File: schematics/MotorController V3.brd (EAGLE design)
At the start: 120.6 x 100 mm, 53 parts, among them IC1 7805, Q1 BC307

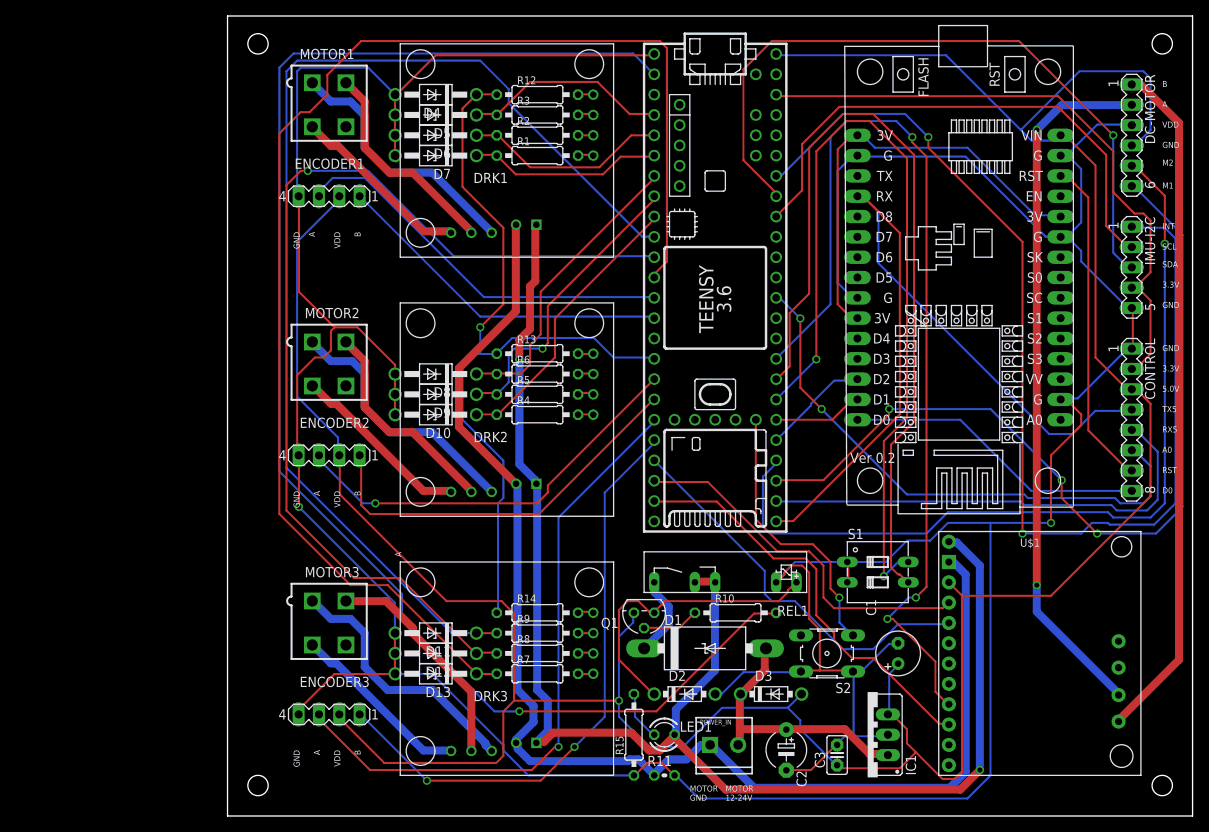
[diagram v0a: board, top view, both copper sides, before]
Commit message: ESP8266 NodeMCU V2 foot print corrected
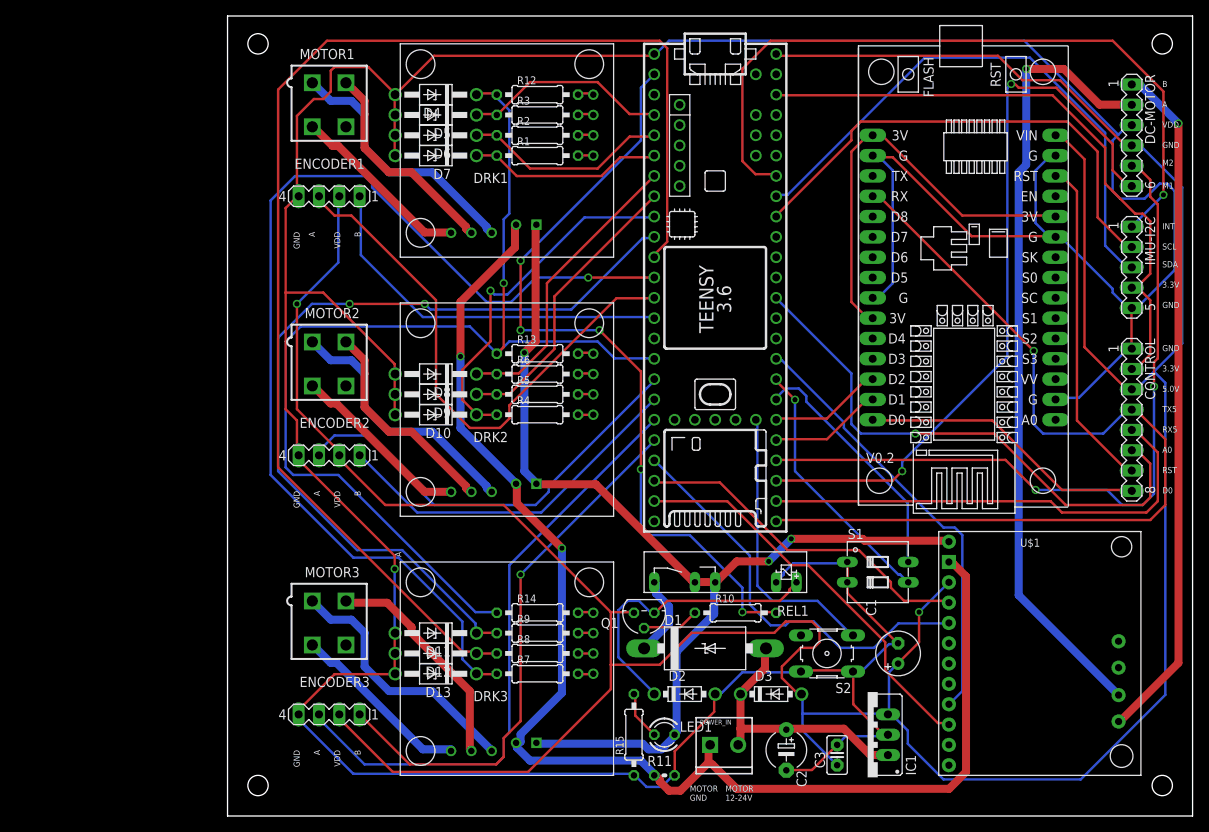
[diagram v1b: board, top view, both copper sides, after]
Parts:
- moved U$3 0.63 mm to (14.6, 53.3)
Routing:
- net N$42: track 180.6 -> 98.5 mm, vias 1 -> 5
- net N$40: track 105.1 -> 30.9 mm, vias 2 -> 0
- net N$12: track 103.3 -> 32.4 mm, vias 0 -> 1
- net N$60: track 120.2 -> 54.8 mm, vias 3 -> 0
- net LIPO-VDD: track 184.1 -> 132.3 mm, vias 2 -> 3
- net IMU-INT: track 137.9 -> 91.8 mm, vias 2 -> 1
- net +5V: track 380.7 -> 422.6 mm, vias 1 -> 2
- net N$46: track 98.7 -> 135.9 mm
- net N$28: track 125.6 -> 162.7 mm, vias 1 -> 0
- net N$27: track 141.1 -> 106.0 mm, vias 0 -> 2
- net N$29: track 167.4 -> 133.0 mm, vias 0 -> 1
- net ENC1_A: track 49.4 -> 68.8 mm
- net IMU-SDA: track 87.9 -> 70.9 mm, vias 1 -> 0
- net WH_ENC_B: track 107.0 -> 92.6 mm, vias 3 -> 2
- net GND: track 516.2 -> 503.0 mm, vias 2 -> 1
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
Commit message: calibrated PID of lifter motor
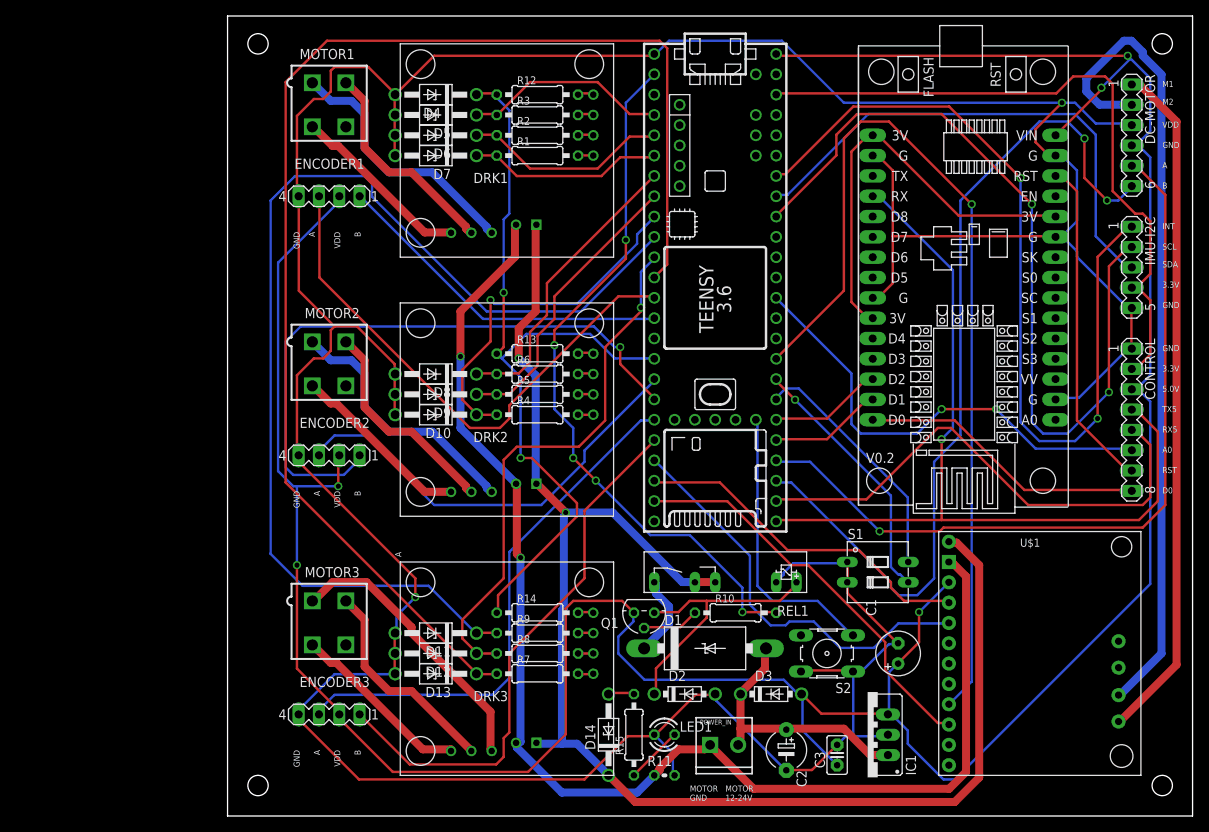
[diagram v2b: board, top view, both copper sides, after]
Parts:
- added D14: 5.6V, diode:DO41Z10
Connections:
- removed net N$41: LED1.A, R15.2
- new net N$33: D14.A, R15.2
- new net N$34: LED1.K, R15.1
- net GND: now also LED1.A; no longer R15.1
- net LIPO-VDD: now also D14.C; no longer LED1.K
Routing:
- net N$28: track 162.7 -> 67.3 mm, vias 0 -> 1
- net N$60: track 54.8 -> 115.9 mm, vias 0 -> 1
- net LIPO-VDD: track 132.3 -> 182.0 mm, vias 3 -> 2
- net IMU-SCL: track 61.5 -> 102.7 mm, vias 0 -> 2
- net N$46: track 135.9 -> 99.6 mm, vias 1 -> 2
- net ENC2_B: track 45.6 -> 78.6 mm, vias 0 -> 1
- net N$29: track 133.0 -> 165.9 mm, vias 1 -> 0
- net GND: track 503.0 -> 470.7 mm, vias 1 -> 2
- net +5V: track 422.6 -> 390.5 mm, vias 2 -> 5
- net N$27: track 106.0 -> 137.7 mm, vias 2 -> 0
- net WH_ENC_B: track 92.6 -> 109.0 mm
- net IMU-INT: track 91.8 -> 106.3 mm, vias 1 -> 2
- net A0: track 68.8 -> 58.7 mm, vias 1 -> 2
- net ENC3_A: track 76.3 -> 66.7 mm
- net N$42: track 98.5 -> 89.3 mm
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
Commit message: no message
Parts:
- removed U$3: NODEMCUNODEMCUV2, nodemcu:NODEMCUV2
- added U$2: NODEMCUNODEMCUV2, nodemcu:NODEMCUV2
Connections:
- net +5V: now also IMU-I2C.4, U$2.30; no longer U$3.15
- net 3.3V: now also IMU-I2C.5; no longer IMU-I2C.4
- net 3V: now also U$2.11, U$2.16; no longer U$3.11, U$3.16, U$3.25
- net D0: now also U$2.15; no longer U$3.30
- net GND: now also U$2.10, U$2.17, U$2.2, U$2.24, U$2.25, U$2.29, U$2.9; no longer IMU-I2C.5, U$3.10, U$3.14, U$3.17, U$3.2, U$3.24
- net RST: now also U$2.28; no longer U$3.13
- net SCL1: now also U$2.13; no longer U$3.28
- net SDA1: now also U$2.14; no longer U$3.29
- net TX5: now also U$2.4; no longer U$3.19
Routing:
- net N$29: track 165.9 -> 65.9 mm, vias 0 -> 2
- net N$12: track 32.4 -> 112.0 mm, vias 1 -> 0
- net GND: track 470.7 -> 414.8 mm, vias 2 -> 0
- net N$42: track 89.3 -> 137.7 mm, vias 5 -> 3
- net IMU-SCL: track 102.7 -> 64.1 mm, vias 2 -> 0
- net N$28: track 67.3 -> 103.9 mm, vias 1 -> 2
- net ENC2_B: track 78.6 -> 45.6 mm, vias 1 -> 0
- net N$27: track 137.7 -> 105.1 mm, vias 0 -> 2
- net +5V: track 390.5 -> 412.4 mm, vias 5 -> 2
- net IMU-INT: track 106.3 -> 92.2 mm, vias 2 -> 3
- net N$60: track 115.9 -> 128.5 mm, vias 1 -> 0
- net WH_ENC_B: track 109.0 -> 97.8 mm, vias 2 -> 1
- net BLCK-M2: track 101.3 -> 111.7 mm
- net RST: track 41.6 -> 49.8 mm, vias 0 -> 1
- net RX5: track 64.7 -> 57.0 mm
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
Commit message: no message
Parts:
- moved U$2 112.1 mm to (21.6, 50.2), turned to 180 degrees
- moved MOTOR1 90.7 mm to (-17.1, -3.81), turned to 0 degrees
- moved POWER_IN 83.2 mm to (0.00, 76.8)
- moved MOTOR2 77.1 mm to (-0.64, -3.81), turned to 0 degrees
- moved ENCODER1 72.7 mm to (-16.5, 6.99), turned to 0 degrees
- moved R15 71.3 mm to (5.71, 61.0), turned to 270 degrees
- moved D3 68.5 mm to (1.91, 69.2), turned to 180 degrees
- moved ENCODER2 66.7 mm to (0.00, 6.99), turned to 0 degrees
- moved IC1 64.7 mm to (-14.6, 57.8), turned to 0 degrees
- moved LED1 63.9 mm to (-3.17, 57.8)
- moved D14 61.3 mm to (0.64, 50.8), turned to 0 degrees
- moved R11 57.8 mm to (-8.26, 47.6), turned to 180 degrees
- moved CONTROL 55.1 mm to (-10.2, 62.2), turned to 0 degrees
- moved IMU-I2C 54.4 mm to (-14.0, 70.5), turned to 0 degrees
- moved C2 53.9 mm to (-16.5, 47.0), turned to 0 degrees
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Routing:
- net GND: track 414.8 -> 0.00 mm
- net +5V: track 412.4 -> 0.00 mm, vias 2 -> 0
- net LIPO-VDD: track 182.0 -> 0.00 mm, vias 2 -> 0
- net LIPO-GND: track 163.5 -> 0.00 mm, vias 2 -> 0
- net N$42: track 137.7 -> 0.00 mm, vias 3 -> 0
- net N$60: track 128.5 -> 0.00 mm
- net TX5: track 114.4 -> 0.00 mm
- net N$12: track 112.0 -> 0.00 mm
- net BLCK-M2: track 111.7 -> 0.00 mm
- net N$27: track 105.1 -> 0.00 mm, vias 2 -> 0
- net N$28: track 103.9 -> 0.00 mm, vias 2 -> 0
- net Y_ENC_A: track 100.2 -> 0.00 mm, vias 3 -> 0
- net WH_ENC_B: track 97.8 -> 0.00 mm, vias 1 -> 0
- net N$46: track 97.6 -> 0.00 mm, vias 1 -> 0
- net IMU-INT: track 92.2 -> 0.00 mm, vias 3 -> 0
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
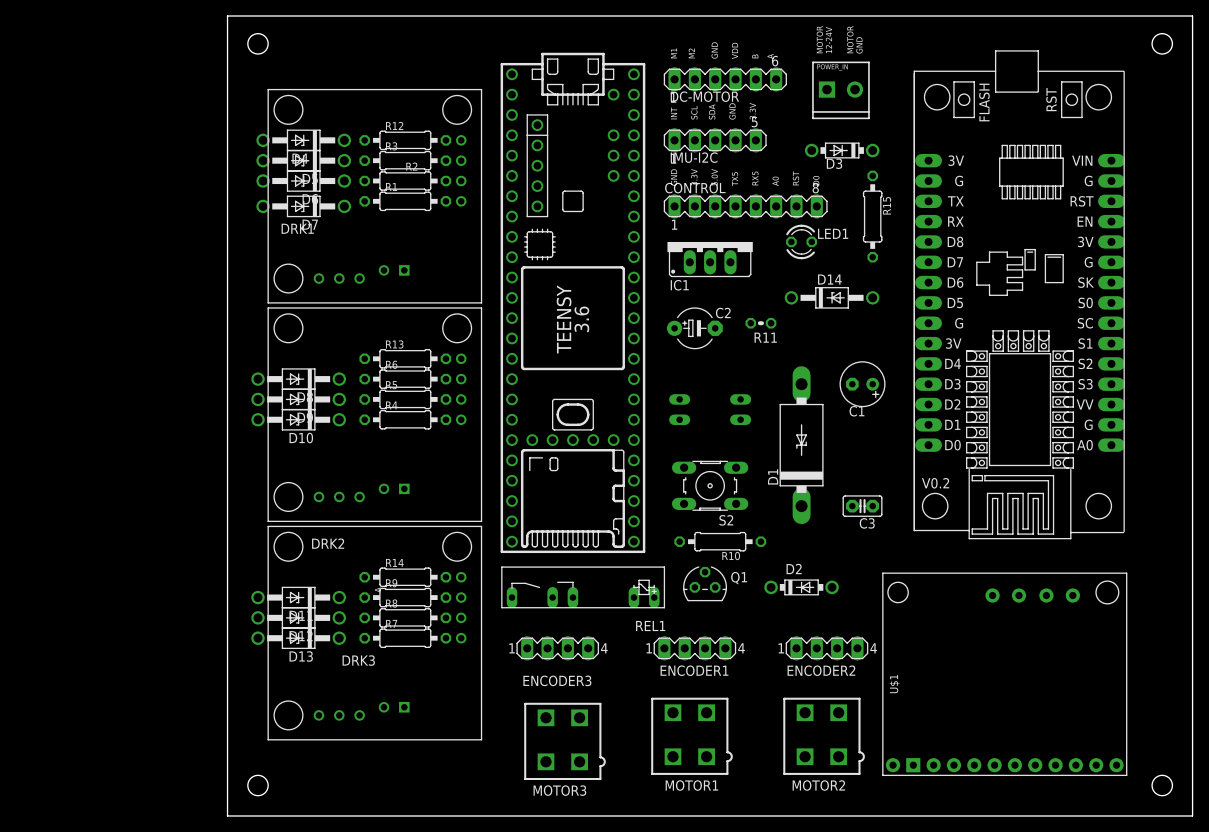
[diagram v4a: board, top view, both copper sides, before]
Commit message: more aggressive Motor PID
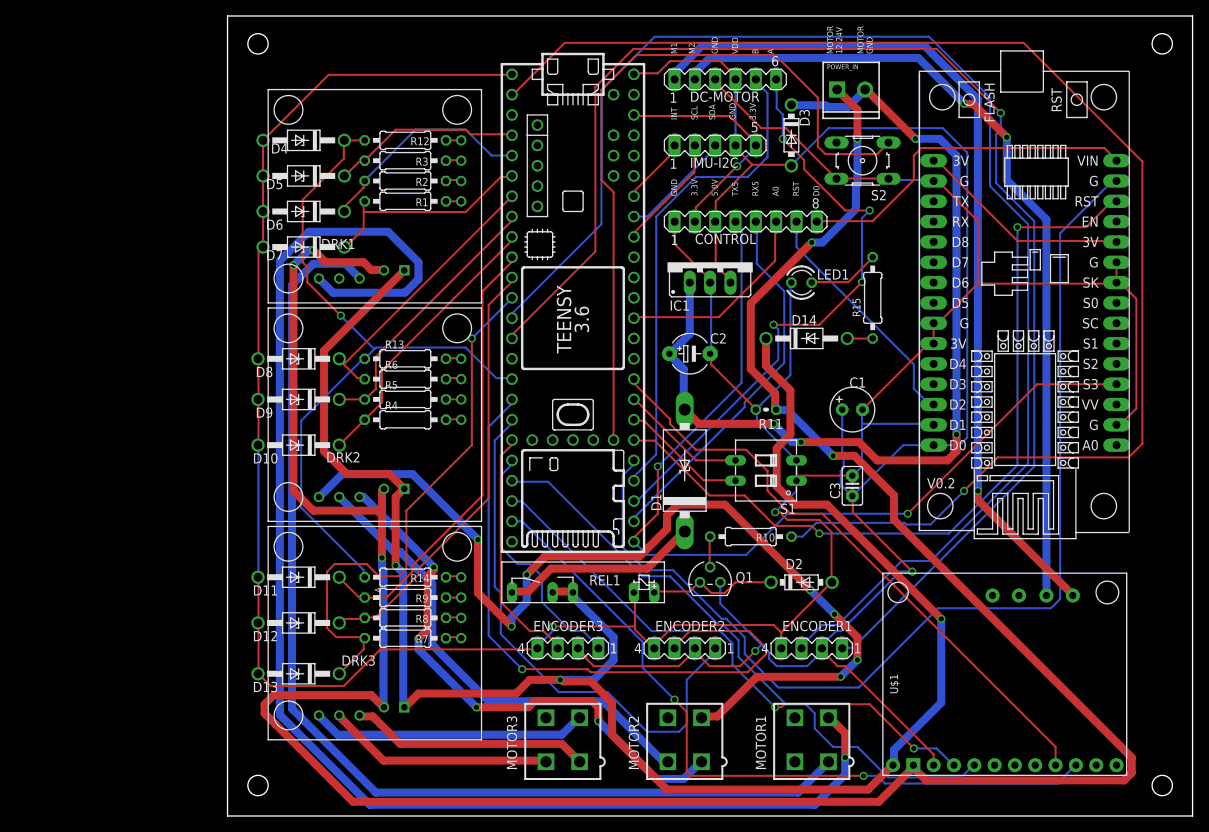
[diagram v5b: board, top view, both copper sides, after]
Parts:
- R4, R5, R6, R7, R8, R9: value 330 -> 1K
- moved S2 44.9 mm to (4.45, 67.9)
- moved ENCODER2 17.8 mm to (-17.8, 6.99), turned to 180 degrees
- moved MOTOR2 17.2 mm to (-17.8, -4.45)
- moved MOTOR1 15.3 mm to (-1.91, -4.45)
- moved D1 14.9 mm to (-17.8, 29.2)
- moved ENCODER1 14.6 mm to (-1.91, 6.99), turned to 180 degrees
- moved R11 10.8 mm to (-7.62, 36.8)
- moved S1 10.3 mm to (-7.62, 29.2), flipped to the top
- moved R15 10.2 mm to (5.71, 50.8)
- moved D3 6.63 mm to (-4.45, 71.1), turned to 270 degrees
- moved D14 5.99 mm to (-2.54, 45.7)
- moved D7 5.08 mm to (-65.4, 57.1)
- moved LED1 5.08 mm to (-3.17, 52.7)
- moved D13 4.45 mm to (-66.0, 3.81)
- moved R10 3.86 mm to (-9.53, 21.0), turned to 0 degrees
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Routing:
- net GND: track 0.00 -> 402.1 mm, vias 0 -> 2
- net LIPO-GND: track 0.00 -> 329.4 mm, vias 0 -> 6
- net +5V: track 0.00 -> 235.1 mm, vias 0 -> 2
- net LIPO-VDD: track 0.00 -> 228.6 mm, vias 0 -> 3
- net N$1: track 0.00 -> 178.1 mm, vias 0 -> 1
- net ENC1_A: track 0.00 -> 173.4 mm
- net N$42: track 0.00 -> 171.7 mm, vias 0 -> 1
- net ENC1_B: track 0.00 -> 171.6 mm, vias 0 -> 1
- net N$3: track 0.00 -> 136.3 mm
- net SDA1: track 0.00 -> 134.7 mm
- net N$13: track 0.00 -> 122.5 mm, vias 0 -> 7
- net N$32: track 0.00 -> 116.8 mm, vias 0 -> 4
- net TX5: track 0.00 -> 115.8 mm, vias 0 -> 2
- net RED-M1: track 0.00 -> 109.8 mm, vias 0 -> 1
- net BLCK-M2: track 0.00 -> 104.1 mm, vias 0 -> 2
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
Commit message: aligned coord systems of IMU and kinematics
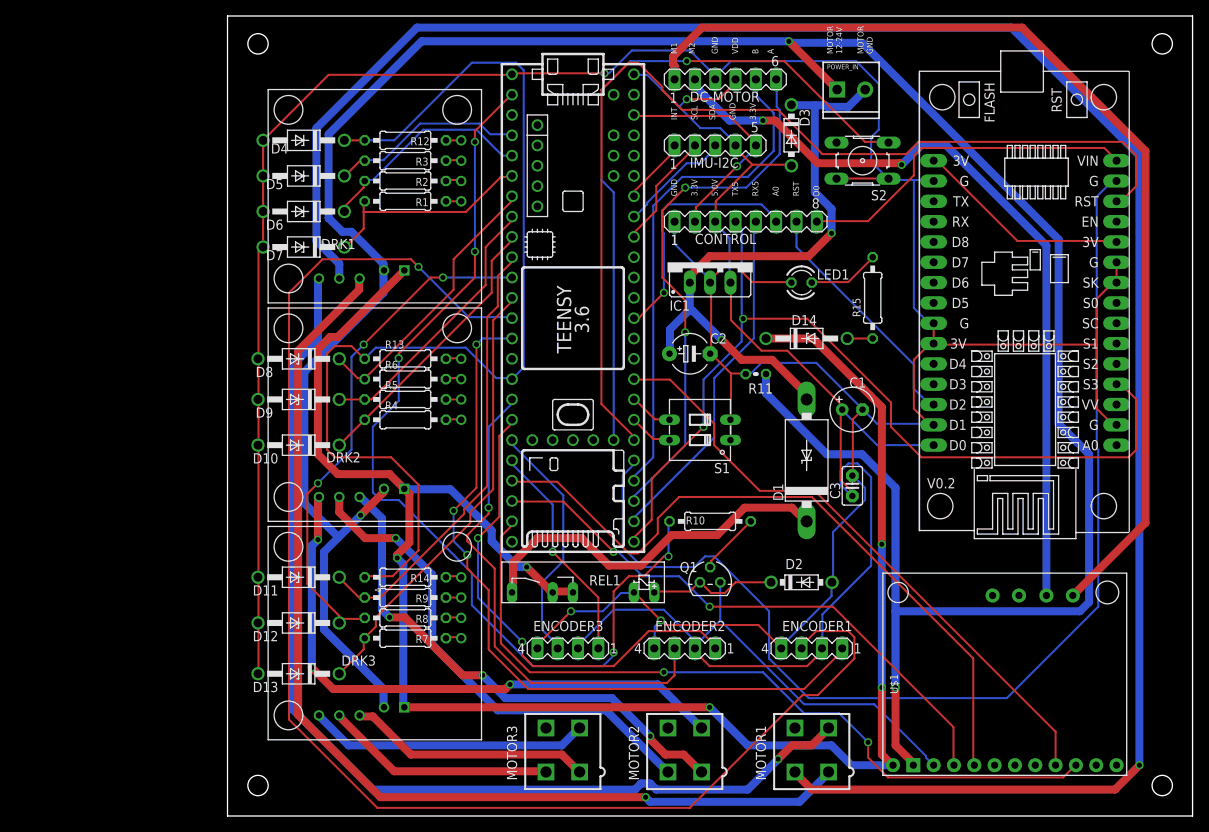
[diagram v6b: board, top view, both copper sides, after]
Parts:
- moved D1 15.3 mm to (-2.54, 30.5)
- moved S1 9.69 mm to (-15.9, 34.3)
- moved R10 5.43 mm to (-14.6, 22.9), turned to 180 degrees
- moved R11 4.62 mm to (-8.89, 41.3)
- moved MOTOR1 1.27 mm to (-1.91, -5.71)
- moved MOTOR2 1.27 mm to (-17.8, -5.71)
- moved MOTOR3 1.27 mm to (-33.0, -5.71)
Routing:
- net N$2: track 0.00 -> 256.2 mm, vias 0 -> 1
- net ENC1_B: track 171.6 -> 94.4 mm, vias 1 -> 3
- net N$42: track 171.7 -> 120.1 mm, vias 1 -> 5
- net N$13: track 122.5 -> 74.1 mm, vias 7 -> 3
- net N$1: track 178.1 -> 130.3 mm
- net N$46: track 89.2 -> 134.0 mm, vias 1 -> 0
- net N$32: track 116.8 -> 77.5 mm, vias 4 -> 2
- net SCL1: track 99.8 -> 127.1 mm, vias 2 -> 0
- net N$39: track 24.7 -> 46.9 mm
- net +5V: track 235.1 -> 213.6 mm, vias 2 -> 1
- net ENC2_A: track 82.4 -> 62.8 mm
- net RED-M1: track 109.8 -> 129.2 mm, vias 1 -> 0
- net N$29: track 68.7 -> 55.9 mm, vias 1 -> 0
- net N$44: track 76.1 -> 87.3 mm
- net N$28: track 54.5 -> 65.2 mm, vias 0 -> 3
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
